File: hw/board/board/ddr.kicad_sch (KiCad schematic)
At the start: 2 parts

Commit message: Start work on ddr
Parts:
- removed U1: ~, Package_BGA:BGA-400_17.0x17.0mm_Layout20x20_P0.8mm, symbol IC:T20F400
- added R10, R11, R12, R13, R14, R15, R16, R17, R18, R8, R9: 15R, Resistor_SMD:R_0402_1005Metric, symbol Device:R
- added R19: 240R, Resistor_SMD:R_0402_1005Metric, symbol Device:R
- added R20, R21: 1k, Resistor_SMD:R_0402_1005Metric, symbol Device:R
- added R22, R23, R24, R25, R26, R27, R28, R29, R30, R31, R32, R33, R34, R35, R36, R37, R38, R39, R40, R41, R42, R43, R44, R45: 40R, Resistor_SMD:R_0402_1005Metric, symbol Device:R
- added R7: 100R, Resistor_SMD:R_0402_1005Metric, symbol Device:R
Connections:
- net at U8.B3 (DQ0): now also R8.2
- net at U8.B7 (DM/TDQS): now also R18.2
- net at U8.C2 (DQ2): now also R10.2
- net at U8.C3 (DQS): now also R16.2
- net at U8.C7 (DQ1): now also R9.2
- net at U8.C8 (DQ3): now also R11.2
- net at U8.D2 (DQ6): now also R14.2
- net at U8.D3 (DQS#): now also R17.2
- net at U8.E3 (DQ4): now also R12.2
- net at U8.E7 (DQ7): now also R15.2
- net at U8.E8 (DQ5): now also R13.2
- net DDR_RAS#: now reaches U8.F3 (RAS#)
- net DDR_RAS#: now also R43.2
- net DDR_CK: now reaches U8.F7 (CK)
- net DDR_CK: now also R7.1
- net DDR_ODT: now reaches U8.G1 (ODT)
- net DDR_ODT: now also R45.2
- net DDR_CAS#: now reaches U8.G3 (CAS#)
- net DDR_CAS#: now also R42.2
- net DDR_CK#: now reaches U8.G7 (CK#)
- net DDR_CK#: now also R7.2
- net DDR_CKE: now reaches U8.G9 (CKE)
- net DDR_CKE: now also R40.2
- net DDR_CS#: now reaches U8.H2 (CS#)
- net DDR_CS#: now also R44.2
- net DDR_WE#: now reaches U8.H3 (WE#)
- net DDR_WE#: now also R41.2
- net DDR_A10: now reaches U8.H7 (A10/AP)
- net DDR_A10: now also R32.2
- net at U8.H8 (ZQ): now also R19.1
- net DDR_BA0: now reaches U8.J2 (BA0)
- net DDR_BA0: now also R37.2
- net DDR_BA2: now reaches U8.J3 (BA2)
- net DDR_BA2: now also R39.2
- net DDR_A3: now reaches U8.K2 (A3)
- net DDR_A3: now also R25.2
- net DDR_A0: now reaches U8.K3 (A0)
- net DDR_A0: now also R22.2
- net DDR_A12: now reaches U8.K7 (A12/BC#)
- net DDR_A12: now also R34.2
- net DDR_BA1: now reaches U8.K8 (BA1)
- net DDR_BA1: now also R38.2
- net DDR_A5: now reaches U8.L2 (A5)
- net DDR_A5: now also R27.2
- net DDR_A2: now reaches U8.L3 (A2)
- net DDR_A2: now also R24.2
- net DDR_A1: now reaches U8.L7 (A1)
- net DDR_A1: now also R23.2
- net DDR_A4: now reaches U8.L8 (A4)
- net DDR_A4: now also R26.2
- net DDR_A7: now reaches U8.M2 (A7)
- net DDR_A7: now also R29.2
- net DDR_A9: now reaches U8.M3 (A9)
- net DDR_A9: now also R31.2
- net DDR_A11: now reaches U8.M7 (A11)
- net DDR_A11: now also R33.2
- net DDR_A6: now reaches U8.M8 (A6)
- net DDR_A6: now also R28.2
- net DDR_RESET#: now reaches U8.N2 (RESET#)
- net DDR_A13: now reaches U8.N3 (A13)
- net DDR_A13: now also R35.2
- net DDR_A14: now reaches U8.N7 (A14)
- net DDR_A14: now also R36.2
- net DDR_A8: now reaches U8.N8 (A8)
- net DDR_A8: now also R30.2
- net GND: now reaches U8.A1 (VSS)
- net GND: now also U8.A8 (VSS), U8.B1 (VSS), U8.B2 (VSSQ), U8.B8 (VSSQ), U8.C9 (VSSQ), U8.D1 (VSSQ), U8.D8 (VSS), U8.D9 (VSSQ), U8.F2 (VSS), U8.F8 (VSS), U8.J1 (VSS), U8.J9 (VSS), U8.L1 (VSS), U8.L9 (VSS), U8.N1 (VSS), U8.N9 (VSS), R19.2, R21.2
- net +1V35: now reaches U8.A2 (VDD)
- net +1V35: now also U8.A9 (VDD), U8.B9 (VDDQ), U8.C1 (VDDQ), U8.D7 (VDD), U8.E2 (VDDQ), U8.E9 (VDDQ), U8.G2 (VDD), U8.G8 (VDD), U8.K1 (VDD), U8.K9 (VDD), U8.M1 (VDD), U8.M9 (VDD), R20.1
- net VTT: now reaches U8.E1 (VREFDQ)
- net VTT: now also U8.J8 (VREFCA), R20.2, R21.1, R22.1, R23.1, R24.1, R25.1, R26.1, R27.1, R28.1, R29.1, R30.1, R31.1, R32.1, R33.1, R34.1, R35.1, R36.1, R37.1, R38.1, R39.1, R40.1, R41.1, R42.1, R43.1, R44.1, R45.1
- new net DDR_DM: R18.1
- new net DDR_DQ0: R8.1
- new net DDR_DQ1: R9.1
- new net DDR_DQ2: R10.1
- new net DDR_DQ3: R11.1
- new net DDR_DQ4: R12.1
- new net DDR_DQ5: R13.1
- new net DDR_DQ6: R14.1
- new net DDR_DQ7: R15.1
- new net DDR_DQS: R16.1
- new net DDR_DQS#: R17.1
- no-connect marks 0 -> 1
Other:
- moved on the sheet: U8B

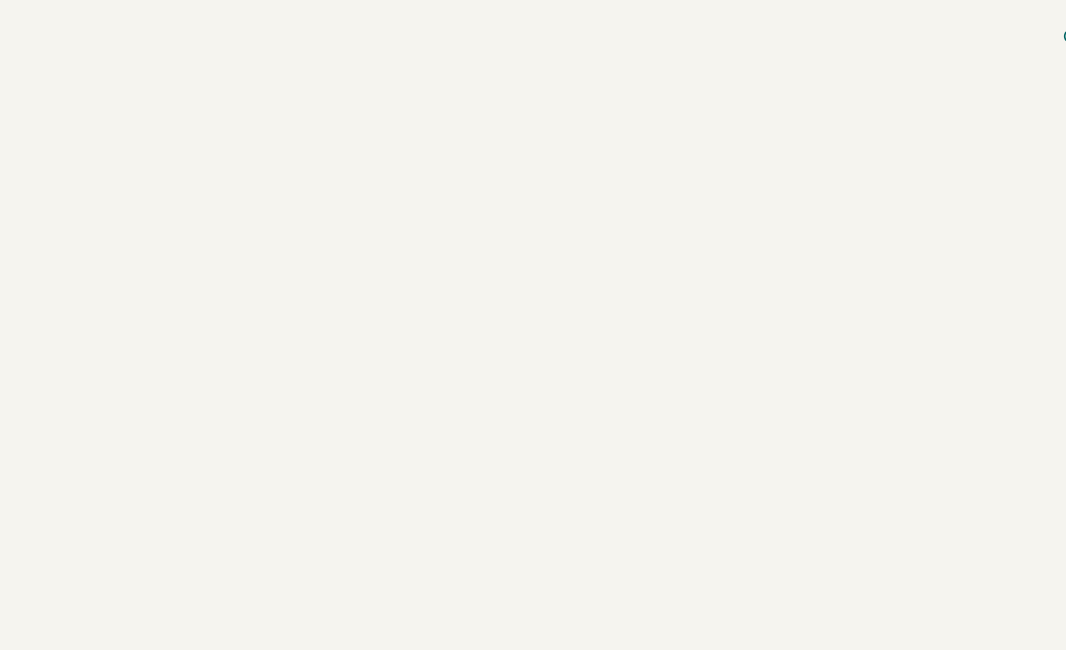
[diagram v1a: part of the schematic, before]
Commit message: Add decoupling capacitors
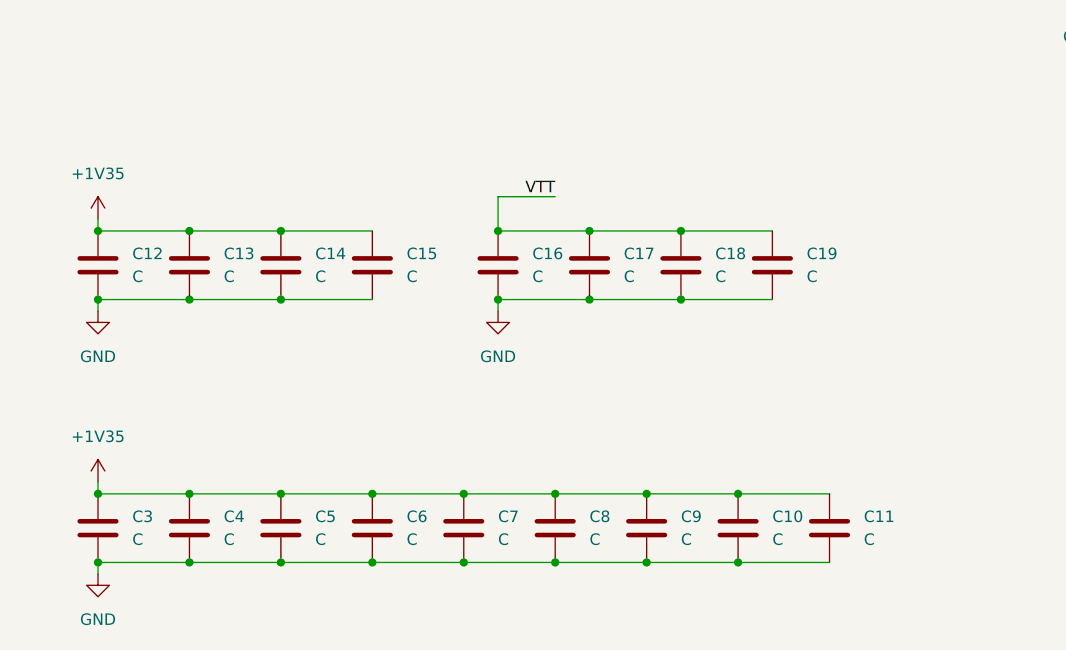
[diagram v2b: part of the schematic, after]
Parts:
- added C10, C11, C12, C13, C14, C15, C16, C17, C18, C19, C3, C4, C5, C6, C7, C8, C9: C, Capacitor_SMD:C_0402_1005Metric, symbol Device:C
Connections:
- net +1V35: now also C10.1, C11.1, C12.1, C13.1, C14.1, C15.1, C3.1, C4.1, C5.1, C6.1, C7.1, C8.1, C9.1
- net GND: now also C10.2, C11.2, C12.2, C13.2, C14.2, C15.2, C16.2, C17.2, C18.2, C19.2, C3.2, C4.2, C5.2, C6.2, C7.2, C8.2, C9.2
- net VTT: now also C16.1, C17.1, C18.1, C19.1
